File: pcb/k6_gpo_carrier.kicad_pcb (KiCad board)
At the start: 2 copper layers, 100 x 100 mm, 22 parts, among them J1 LM2596_Buck, J10 BTN_RESET, J2 XL6009_Boost, J3 12V_IN, J4 PHONE, J5 MAX98357A, J6 DAC_OUT, J7 SD_Card, J8 BTN_RING, J9 BTN_CANCEL, T1 600R_XFMR, U1 ESP32_DevKit, U2 L293D, U3 PC817

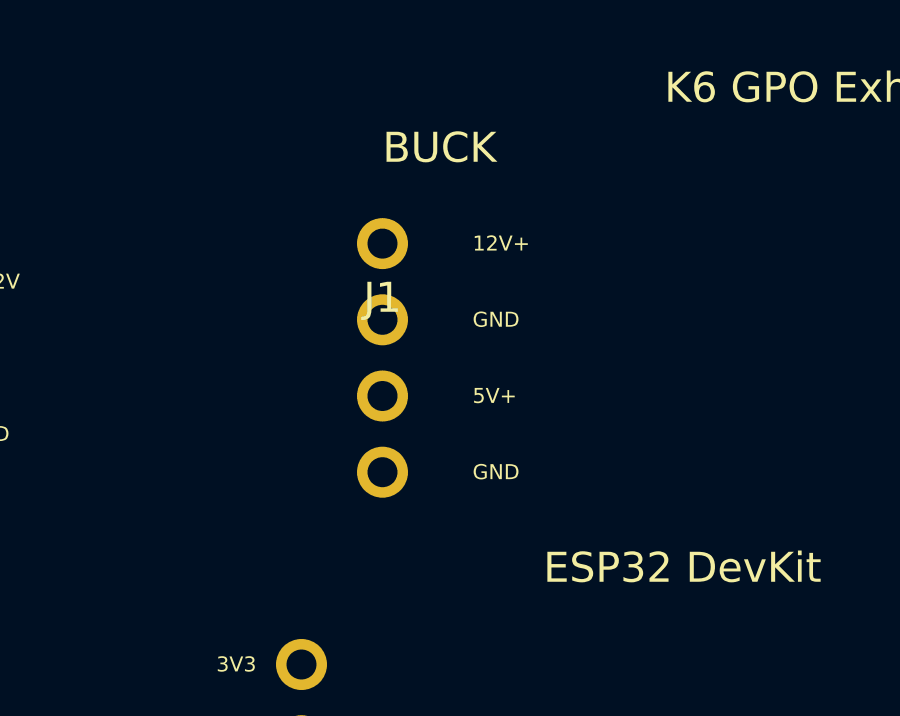
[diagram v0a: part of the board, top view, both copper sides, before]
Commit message: fix: LM2596 buck module updated to 5-pin header (IN+, IN-, OUT+, OUT-, ON/OFF)
Also includes previous fix for KiCad 10 justify=center parse error.

Co-Authored-By: Devin AI <158243242+devin-ai-integration[bot]@users.noreply.github.com>
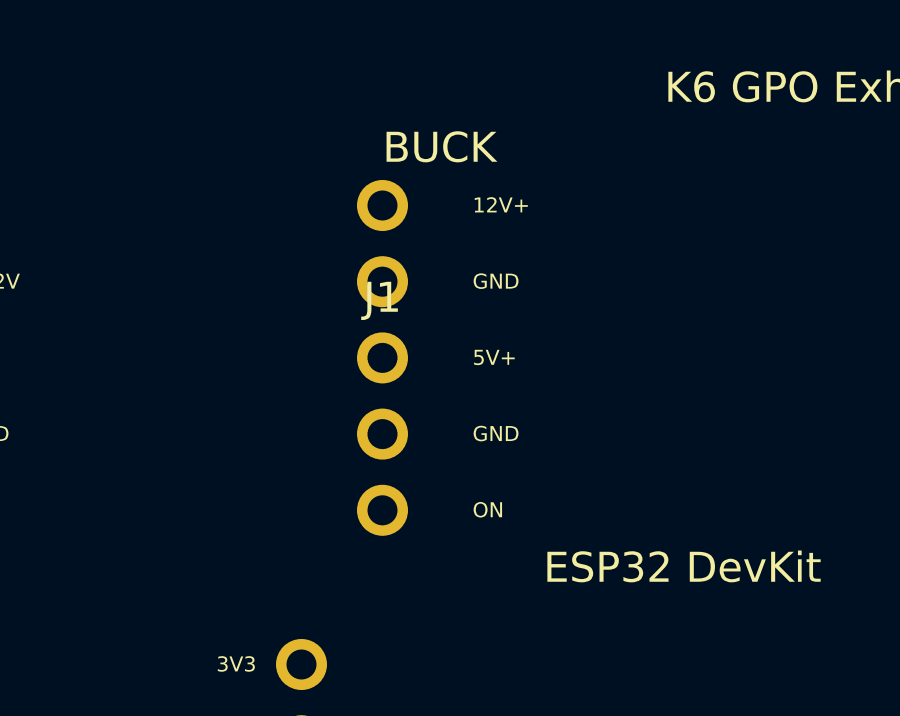
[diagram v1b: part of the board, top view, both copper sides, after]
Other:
- board text added: "ON"
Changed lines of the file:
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@@
     (effects (font (size 1 1) (thickness 0.15)))
 )
-    (fp_rect (start -1.500 -5.580) (end 1.500 5.580) (stroke (width 0.05) (type default)) (fill none) (layer "F.CrtYd"))
-  (pad "1" thru_hole circle (at 0.000 -3.810) (size 1.7 1.7) (drill 1.0) (layers "*.Cu" "*.Mask") (net 1 "+12V"))
-  (pad "2" thru_hole circle (at 0.000 -1.270) (size 1.7 1.7) (drill 1.0) (layers "*.Cu" "*.Mask") (net 4 "GND"))
-  (pad "3" thru_hole circle (at 0.000 1.270) (size 1.7 1.7) (drill 1.0) (layers "*.Cu" "*.Mask") (net 2 "+5V"))
-  (pad "4" thru_hole circle (at 0.000 3.810) (size 1.7 1.7) (drill 1.0) (layers "*.Cu" "*.Mask") (net 4 "GND"))
+    (fp_rect (start -1.500 -6.850) (end 1.500 6.850) (stroke (width 0.05) (type default)) (fill none) (layer "F.CrtYd"))
+  (pad "1" thru_hole circle (at 0.000 -5.080) (size 1.7 1.7) (drill 1.0) (layers "*.Cu" "*.Mask") (net 1 "+12V"))
+  (pad "2" thru_hole circle (at 0.000 -2.540) (size 1.7 1.7) (drill 1.0) (layers "*.Cu" "*.Mask") (net 4 "GND"))
+  (pad "3" thru_hole circle (at 0.000 0.000) (size 1.7 1.7) (drill 1.0) (layers "*.Cu" "*.Mask") (net 2 "+5V"))
+  (pad "4" thru_hole circle (at 0.000 2.540) (size 1.7 1.7) (drill 1.0) (layers "*.Cu" "*.Mask") (net 4 "GND"))
+  (pad "5" thru_hole circle (at 0.000 5.080) (size 1.7 1.7) (drill 1.0) (layers "*.Cu" "*.Mask") (net 0 ""))
   )
   (footprint "K6_GPO:J2" (layer "F.Cu")
@@
     (effects (font (size 1.0 1.0) (thickness 0.15)) (justify left))
 )
-  (gr_text "12V+" (at 161.000 98.190) (layer "F.SilkS")
-    (effects (font (size 0.5 0.5) (thickness 0.1)) (justify left))
-)
-  (gr_text "GND" (at 161.000 100.730) (layer "F.SilkS")
-    (effects (font (size 0.5 0.5) (thickness 0.1)) (justify left))
-)
-  (gr_text "5V+" (at 161.000 103.270) (layer "F.SilkS")
-    (effects (font (size 0.5 0.5) (thickness 0.1)) (justify left))
-)
-  (gr_text "GND" (at 161.000 105.810) (layer "F.SilkS")
-    (effects (font (size 0.5 0.5) (thickness 0.1)) (justify left))
-)
+  (gr_text "12V+" (at 161.000 96.920) (layer "F.SilkS")
+    (effects (font (size 0.5 0.5) (thickness 0.1)) (justify left))
+)
+  (gr_text "GND" (at 161.000 99.460) (layer "F.SilkS")
+    (effects (font (size 0.5 0.5) (thickness 0.1)) (justify left))
+)
+  (gr_text "5V+" (at 161.000 102.000) (layer "F.SilkS")
+    (effects (font (size 0.5 0.5) (thickness 0.1)) (justify left))
+)
+  (gr_text "GND" (at 161.000 104.540) (layer "F.SilkS")
+    (effects (font (size 0.5 0.5) (thickness 0.1)) (justify left))
+)
+  (gr_text "ON" (at 161.000 107.080) (layer "F.SilkS")
+    (effects (font (size 0.5 0.5) (thickness 0.1)) (justify left))
+)

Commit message: feat: Replace LM2596 module with TO-220-5 IC and full buck converter circuit
- U4: LM2596-5.0 TO-220-5 IC (VIN, SW_OUT, GND, FB, ON/OFF)
- C2: 680µF 25V input capacitor
- L1: 33µH power inductor (SW_OUT → +5V)
- D1: 1N5825 Schottky freewheeling diode
- C3: 220µF 25V output capacitor
- New SW_OUT net for switch node connections
- Dashed silkscreen clearance outlines for:
  - XL6009 boost module (43×21mm)
  - MAX98357A DAC module (19×18mm)
  - Micro-SD card module (25×20mm)
- J5/J6/T1/J4 moved down to avoid XL6009 module zone overlap
- PINOUT.md updated with full LM2596 circuit documentation
- Schematic netlist updated for new components

Co-Authored-By: Devin AI <158243242+devin-ai-integration[bot]@users.noreply.github.com>
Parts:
- removed J1: LM2596_Buck, K6_GPO:J1
- added C2: 680uF, K6_GPO:C2, F.Cu at (148.0, 104.0)
- added C3: 220uF, K6_GPO:C3, F.Cu at (168.0, 114.0)
- added D1: 1N5825, K6_GPO:D1, F.Cu at (158.0, 114.0)
- added L1: 33uH, K6_GPO:L1, F.Cu at (168.0, 104.0)
- added U4: LM2596-5.0, K6_GPO:U4, F.Cu at (158.0, 104.0)
- moved J5 18.0 mm to (212.0, 126.0)
- moved J6 18.0 mm to (222.0, 126.0)
- moved T1 12.0 mm to (220.0, 140.0)
- moved J4 10.0 mm to (222.0, 152.0)
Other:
- board text added: "C2 680µF"
- board text added: "C3 220µF"
- board text added: "D1 1N5825"
- board text added: "FB"
- board text added: "L1 33µH"
- board text added: "LM2596"
- board text added: "SW"
- board text added: "VIN"
- board text added: "XL6009 module"
- board text added: "µSD module"
- board text removed: "5V+"
- board text removed: "BUCK"

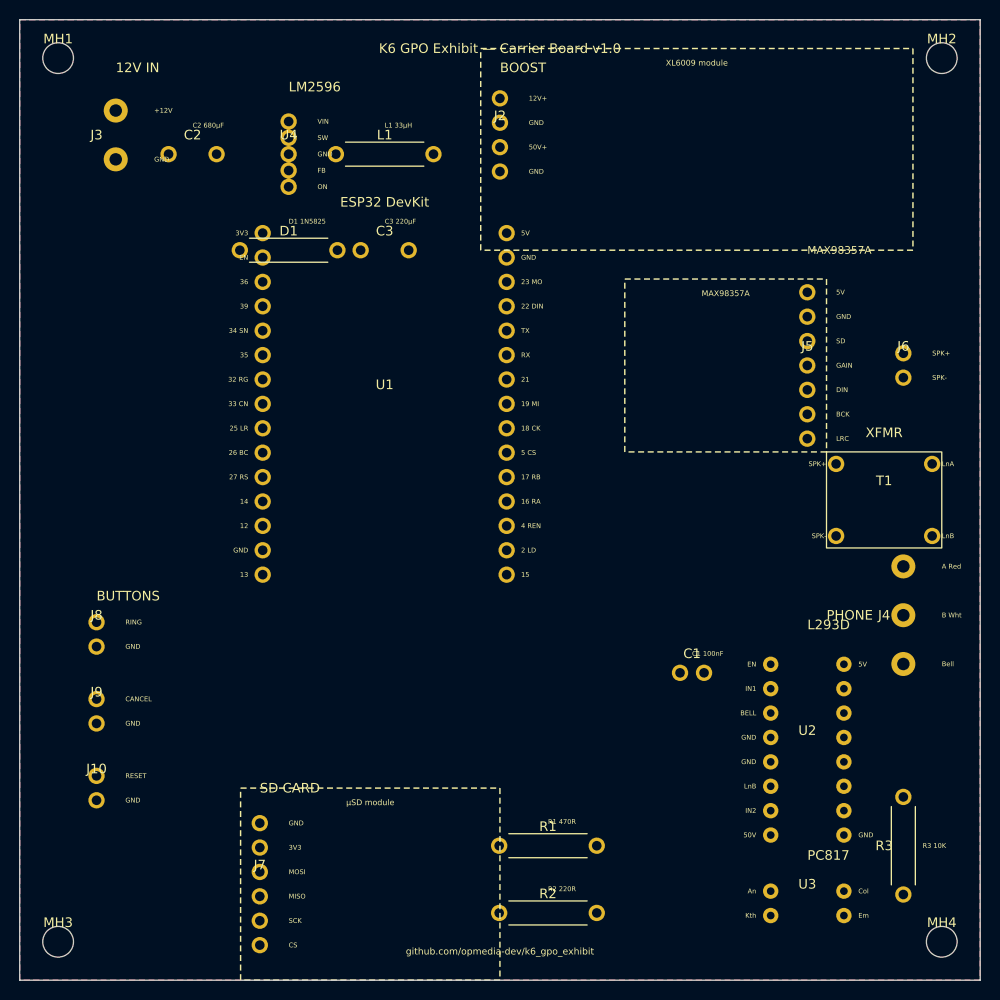
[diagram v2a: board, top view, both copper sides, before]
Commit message: fix: Resolve component overlaps — move D1/C3 away from ESP32 area, separate DAC/XFMR/PHONE spacing
- D1 moved left of ESP32 area (2.2mm clearance to nearest ESP32 pin)
- C3 moved into top row next to L1 (no longer below ESP32)
- J2 (XL6009) shifted right to accommodate C3 in top row
- J6 (DAC out) moved down to y+48, separated from J5 (MAX98357A)
- T1 (XFMR) moved to y+56, J4 (Phone) to y+66 — cascading separation
- Added DAC OUT label for J6

Co-Authored-By: Devin AI <158243242+devin-ai-integration[bot]@users.noreply.github.com>
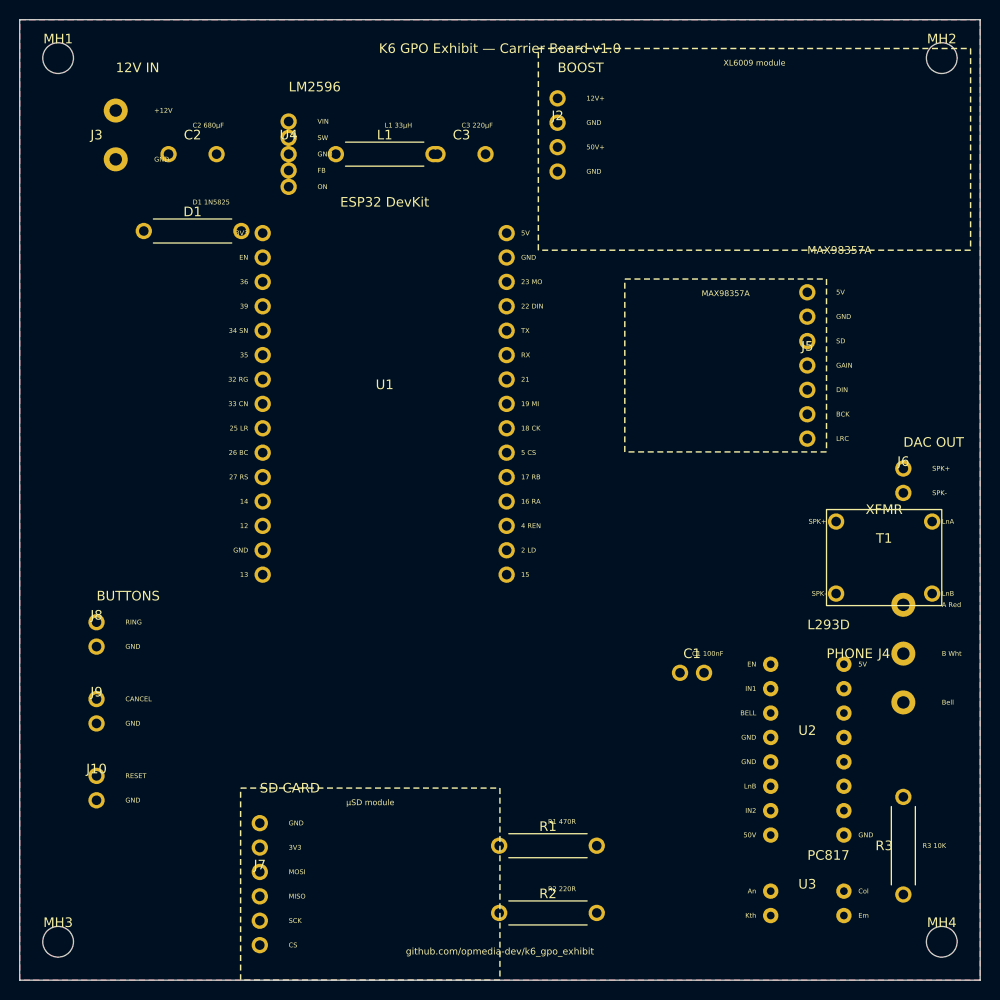
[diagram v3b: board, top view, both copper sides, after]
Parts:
- moved C3 12.8 mm to (176.0, 104.0)
- moved J6 12.0 mm to (222.0, 138.0)
- moved D1 10.2 mm to (148.0, 112.0)
- moved J2 6.00 mm to (186.0, 102.0)
- moved T1 6.00 mm to (220.0, 146.0)
- moved J4 4.00 mm to (222.0, 156.0)
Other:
- board text added: "DAC OUT"
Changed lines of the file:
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@@
   )
   (footprint "K6_GPO:D1" (layer "F.Cu")
-    (at 158.000 114.000 0)
+    (at 148.000 112.000 0)
       (fp_text reference "D1" (at 0.000 -2.000) (layer "F.SilkS")
     (effects (font (size 1 1) (thickness 0.15)))
@@
   )
   (footprint "K6_GPO:C3" (layer "F.Cu")
-    (at 168.000 114.000 0)
+    (at 176.000 104.000 0)
       (fp_text reference "C3" (at 0.000 -2.000) (layer "F.SilkS")
     (effects (font (size 1 1) (thickness 0.15)))
@@
   )
   (footprint "K6_GPO:J2" (layer "F.Cu")
-    (at 180.000 102.000 0)
+    (at 186.000 102.000 0)
       (fp_text reference "J2" (at 0.000 -2.000) (layer "F.SilkS")
     (effects (font (size 1 1) (thickness 0.15)))
@@
   )
   (footprint "K6_GPO:J4" (layer "F.Cu")
-    (at 222.000 152.000 90)
+    (at 222.000 156.000 90)
       (fp_text reference "J4" (at 0.000 -2.000) (layer "F.SilkS")
     (effects (font (size 1 1) (thickness 0.15)))
@@
   )
   (footprint "K6_GPO:J6" (layer "F.Cu")
-    (at 222.000 126.000 0)
+    (at 222.000 138.000 0)
       (fp_text reference "J6" (at 0.000 -2.000) (layer "F.SilkS")
     (effects (font (size 1 1) (thickness 0.15)))
@@
   )
   (footprint "K6_GPO:T1" (layer "F.Cu")
-    (at 220.000 140.000 0)
+    (at 220.000 146.000 0)
       (fp_text reference "T1" (at 0.000 -2.000) (layer "F.SilkS")
     (effects (font (size 1 1) (thickness 0.15)))
@@
     (effects (font (size 0.5 0.5) (thickness 0.1)) (justify left))
 )
-  (gr_text "D1 1N5825" (at 158.000 111.000) (layer "F.SilkS")
-    (effects (font (size 0.5 0.5) (thickness 0.1)) (justify left))
-)
-  (gr_text "C3 220µF" (at 168.000 111.000) (layer "F.SilkS")
-    (effects (font (size 0.5 0.5) (thickness 0.1)) (justify left))
-)
-  (gr_text "BOOST" (at 180.000 95.000) (layer "F.SilkS")
-    (effects (font (size 1.0 1.0) (thickness 0.15)) (justify left))
-)
-  (gr_text "12V+" (at 183.000 98.190) (layer "F.SilkS")
-    (effects (font (size 0.5 0.5) (thickness 0.1)) (justify left))
-)
-  (gr_text "GND" (at 183.000 100.730) (layer "F.SilkS")
-    (effects (font (size 0.5 0.5) (thickness 0.1)) (justify left))
-)
-  (gr_text "50V+" (at 183.000 103.270) (layer "F.SilkS")
-    (effects (font (size 0.5 0.5) (thickness 0.1)) (justify left))
-)
-  (gr_text "GND" (at 183.000 105.810) (layer "F.SilkS")
+  (gr_text "D1 1N5825" (at 148.000 109.000) (layer "F.SilkS")
+    (effects (font (size 0.5 0.5) (thickness 0.1)) (justify left))
+)
+  (gr_text "C3 220µF" (at 176.000 101.000) (layer "F.SilkS")
+    (effects (font (size 0.5 0.5) (thickness 0.1)) (justify left))
+)
+  (gr_text "BOOST" (at 186.000 95.000) (layer "F.SilkS")
+    (effects (font (size 1.0 1.0) (thickness 0.15)) (justify left))
+)
+  (gr_text "12V+" (at 189.000 98.190) (layer "F.SilkS")
+    (effects (font (size 0.5 0.5) (thickness 0.1)) (justify left))
+)
+  (gr_text "GND" (at 189.000 100.730) (layer "F.SilkS")
+    (effects (font (size 0.5 0.5) (thickness 0.1)) (justify left))
+)
+  (gr_text "50V+" (at 189.000 103.270) (layer "F.SilkS")
+    (effects (font (size 0.5 0.5) (thickness 0.1)) (justify left))
+)
+  (gr_text "GND" (at 189.000 105.810) (layer "F.SilkS")
     (effects (font (size 0.5 0.5) (thickness 0.1)) (justify left))
 )
@@
     (effects (font (size 0.5 0.5) (thickness 0.1)) (justify left))
 )
-  (gr_text "SPK+" (at 225.000 124.730) (layer "F.SilkS")
-    (effects (font (size 0.5 0.5) (thickness 0.1)) (justify left))
-)
-  (gr_text "SPK-" (at 225.000 127.270) (layer "F.SilkS")
-    (effects (font (size 0.5 0.5) (thickness 0.1)) (justify left))
-)
-  (gr_text "XFMR" (at 220.000 133.000) (layer "F.SilkS")
+  (gr_text "DAC OUT" (at 222.000 134.000) (layer "F.SilkS")
+    (effects (font (size 1.0 1.0) (thickness 0.15)) (justify left))
+)
+  (gr_text "SPK+" (at 225.000 136.730) (layer "F.SilkS")
+    (effects (font (size 0.5 0.5) (thickness 0.1)) (justify left))
+)
+  (gr_text "SPK-" (at 225.000 139.270) (layer "F.SilkS")
+    (effects (font (size 0.5 0.5) (thickness 0.1)) (justify left))
+)
+  (gr_text "XFMR" (at 220.000 141.000) (layer "F.SilkS")
     (effects (font (size 1.0 1.0) (thickness 0.15)))
 )
-  (gr_text "SPK+" (at 214.000 136.250) (layer "F.SilkS")
-    (effects (font (size 0.5 0.5) (thickness 0.1)) (justify right))
-)
-  (gr_text "SPK-" (at 214.000 143.750) (layer "F.SilkS")
-    (effects (font (size 0.5 0.5) (thickness 0.1)) (justify right))
-)
-  (gr_text "LnA" (at 226.000 136.250) (layer "F.SilkS")
-    (effects (font (size 0.5 0.5) (thickness 0.1)) (justify left))
-)
-  (gr_text "LnB" (at 226.000 143.750) (layer "F.SilkS")
-    (effects (font (size 0.5 0.5) (thickness 0.1)) (justify left))
-)
-  (gr_text "PHONE" (at 214.000 152.000) (layer "F.SilkS")
-    (effects (font (size 1.0 1.0) (thickness 0.15)) (justify left))
-)
-  (gr_text "A Red" (at 226.000 146.920) (layer "F.SilkS")
-    (effects (font (size 0.5 0.5) (thickness 0.1)) (justify left))
-)
-  (gr_text "B Wht" (at 226.000 152.000) (layer "F.SilkS")
-    (effects (font (size 0.5 0.5) (thickness 0.1)) (justify left))
-)
-  (gr_text "Bell" (at 226.000 157.080) (layer "F.SilkS")
+  (gr_text "SPK+" (at 214.000 142.250) (layer "F.SilkS")
+    (effects (font (size 0.5 0.5) (thickness 0.1)) (justify right))
+)
+  (gr_text "SPK-" (at 214.000 149.750) (layer "F.SilkS")
+    (effects (font (size 0.5 0.5) (thickness 0.1)) (justify right))
+)
+  (gr_text "LnA" (at 226.000 142.250) (layer "F.SilkS")
+    (effects (font (size 0.5 0.5) (thickness 0.1)) (justify left))
+)
+  (gr_text "LnB" (at 226.000 149.750) (layer "F.SilkS")
+    (effects (font (size 0.5 0.5) (thickness 0.1)) (justify left))
+)
+  (gr_text "PHONE" (at 214.000 156.000) (layer "F.SilkS")
+    (effects (font (size 1.0 1.0) (thickness 0.15)) (justify left))
+)
+  (gr_text "A Red" (at 226.000 150.920) (layer "F.SilkS")
+    (effects (font (size 0.5 0.5) (thickness 0.1)) (justify left))
+)
+  (gr_text "B Wht" (at 226.000 156.000) (layer "F.SilkS")
+    (effects (font (size 0.5 0.5) (thickness 0.1)) (justify left))
+)
+  (gr_text "Bell" (at 226.000 161.080) (layer "F.SilkS")
     (effects (font (size 0.5 0.5) (thickness 0.1)) (justify left))
 )
@@
     (effects (font (size 0.5 0.5) (thickness 0.1)) (justify left))
 )
-  (gr_line (start 178.000 93.000) (end 223.000 93.000) (stroke (width 0.15) (type dash)) (layer "F.SilkS"))
-  (gr_line (start 223.000 93.000) (end 223.000 114.000) (stroke (width 0.15) (type dash)) (layer "F.SilkS"))
-  (gr_line (start 223.000 114.000) (end 178.000 114.000) (stroke (width 0.15) (type dash)) (layer "F.SilkS"))
-  (gr_line (start 178.000 114.000) (end 178.000 93.000) (stroke (width 0.15) (type dash)) (layer "F.SilkS"))
-  (gr_text "XL6009 module" (at 200.500 94.500) (layer "F.SilkS")
+  (gr_line (start 184.000 93.000) (end 229.000 93.000) (stroke (width 0.15) (type dash)) (layer "F.SilkS"))
+  (gr_line (start 229.000 93.000) (end 229.000 114.000) (stroke (width 0.15) (type dash)) (layer "F.SilkS"))
+  (gr_line (start 229.000 114.000) (end 184.000 114.000) (stroke (width 0.15) (type dash)) (layer "F.SilkS"))
+  (gr_line (start 184.000 114.000) (end 184.000 93.000) (stroke (width 0.15) (type dash)) (layer "F.SilkS"))
+  (gr_text "XL6009 module" (at 206.500 94.500) (layer "F.SilkS")
     (effects (font (size 0.6 0.6) (thickness 0.15)))
 )
